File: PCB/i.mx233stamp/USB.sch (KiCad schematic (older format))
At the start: 36 parts, among them J3 USB_2A, J4 USB_2A, U4 GL850G, U5 RCLAMP0502B, U6 RCLAMP0502B, U7 RCLAMP0502B, U8 RCLAMP0502B, U9 MCP130, X2 12MHz

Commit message: Eliminación de los errores encontrados por el DRC
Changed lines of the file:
@@
-EESchema Schematic File Version 2  date Sat 13 Aug 2011 08:44:42 PM COT
+EESchema Schematic File Version 2  date Sun 14 Aug 2011 07:37:17 PM COT
 LIBS:con-jack
 LIBS:adm3101e
@@
 Sheet 2 4
 Title ""
-Date "14 aug 2011"
+Date "15 aug 2011"
 Rev ""
 Comp ""
@@
 Comment4 ""
 $EndDescr
+Connection ~ 1900 1600
+Connection ~ 1950 2850
+Connection ~ 1950 3150
+Connection ~ 1900 1900
 Text HLabel 2600 5250 0    60   BiDi ~ 0
 USB_P4

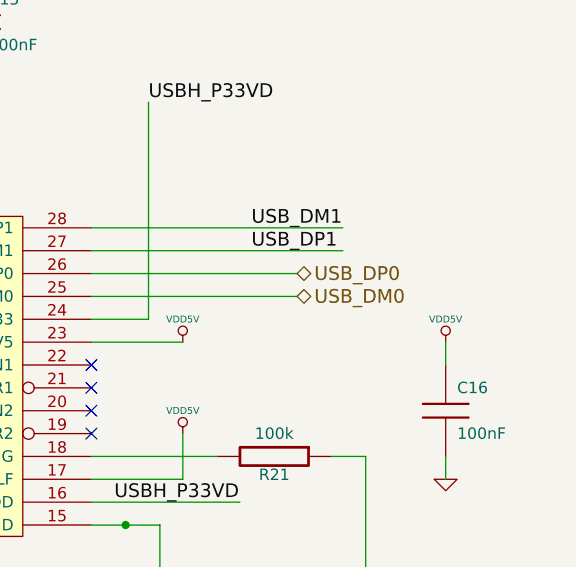
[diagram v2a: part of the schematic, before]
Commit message: Adición de jumpers que permitan el arranque USB
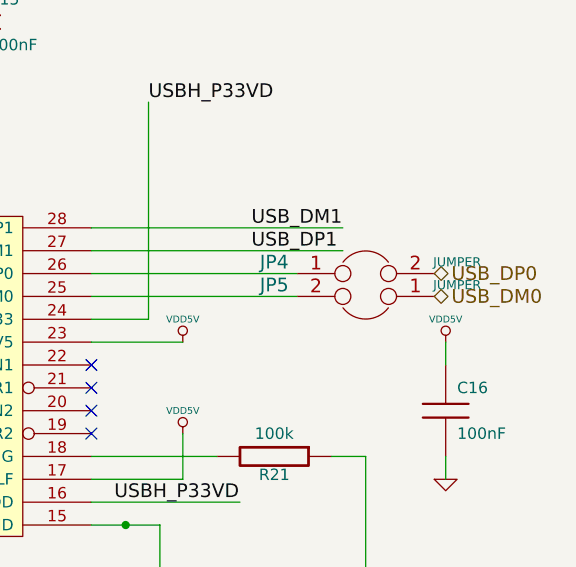
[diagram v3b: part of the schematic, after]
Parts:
- added JP4, JP5: JUMPER, PIN_ARRAY_2X1, symbol JUMPER

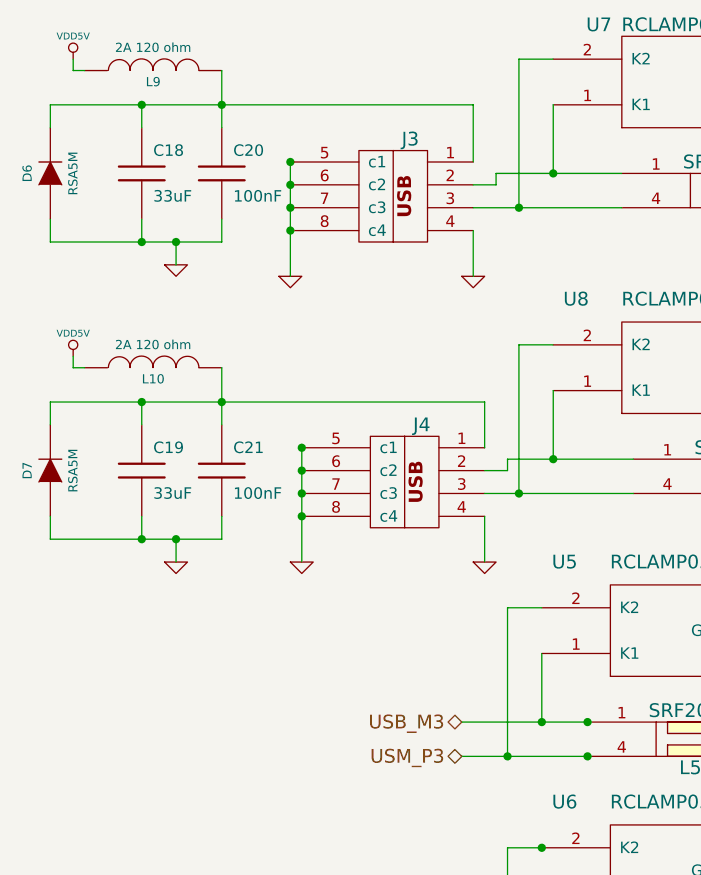
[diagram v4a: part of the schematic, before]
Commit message: LED0603 footprint has been fixed
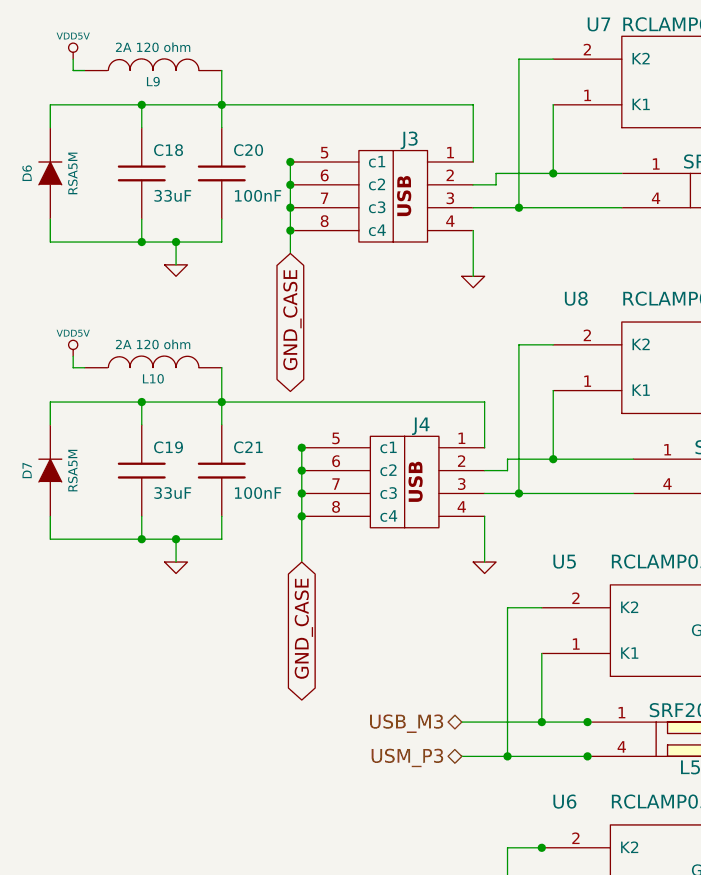
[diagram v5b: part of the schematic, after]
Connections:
- net labels added: GND_CASE
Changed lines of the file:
@@
-EESchema Schematic File Version 2  date Wed 17 Aug 2011 08:52:32 AM COT
+EESchema Schematic File Version 2  date Wed 17 Aug 2011 11:31:08 PM COT
 LIBS:con-jack
 LIBS:adm3101e
@@
 Sheet 2 4
 Title ""
-Date "17 aug 2011"
+Date "18 aug 2011"
 Rev ""
 Comp ""
@@
 Comment4 ""
 $EndDescr
+Wire Wire Line
+	1900 1600 1900 2000
 Connection ~ 1900 1600
 Connection ~ 1950 2850
@@
 Connection ~ 1900 1800
 Connection ~ 1900 1700
-Wire Wire Line
-	1900 1600 1900 2100
 Wire Wire Line
 	2700 1700 2800 1700
@@
 	5800 3550 5850 3550
 Connection ~ 5850 3550
+Text GLabel 1900 2000 3    60   BiDi ~ 0
+GND_CASE
+Text GLabel 1950 3350 3    60   BiDi ~ 0
+GND_CASE
 $Comp
 L JUMPER JP5
@@
 	1    0    0    -1
 $EndComp
-$Comp
-L GND #PWR02
-U 1 1 4E41CF8D
-P 1950 3350
-F 0 "#PWR02" H 1950 3350 30  0001 C CNN
-F 1 "GND" H 1950 3280 30  0001 C CNN
-	1    1950 3350
-	1    0    0    -1
-$EndComp
-$Comp
-L GND #PWR03
-U 1 1 4E41CF53
-P 1900 2100
-F 0 "#PWR03" H 1900 2100 30  0001 C CNN
-F 1 "GND" H 1900 2030 30  0001 C CNN
-	1    1900 2100
-	1    0    0    -1
-$EndComp
 Text Label 7150 3650 0    60   ~ 0
 USBH_P33VD
 $Comp
-L GND #PWR04
+L GND #PWR02
 U 1 1 4E41C8A5
 P 7300 3400
-F 0 "#PWR04" H 7300 3400 30  0001 C CNN
+F 0 "#PWR02" H 7300 3400 30  0001 C CNN
 F 1 "GND" H 7300 3330 30  0001 C CNN
 	1    7300 3400
@@
 $EndComp
 $Comp
-L GND #PWR05
+L GND #PWR03
 U 1 1 4E41C7BC
 P 6100 3800
-F 0 "#PWR05" H 6100 3800 30  0001 C CNN
+F 0 "#PWR03" H 6100 3800 30  0001 C CNN
 F 1 "GND" H 6100 3730 30  0001 C CNN
 	1    6100 3800
@@
 $EndComp
 $Comp
-L GND #PWR06
+L GND #PWR04
 U 1 1 4E4157F8
 P 4250 4850
-F 0 "#PWR06" H 4250 4850 30  0001 C CNN
+F 0 "#PWR04" H 4250 4850 30  0001 C CNN
 F 1 "GND" H 4250 4780 30  0001 C CNN
 	1    4250 4850
@@
 $EndComp
 $Comp
-L GND #PWR07
+L GND #PWR05
 U 1 1 4E4157E9
 P 4250 3800
-F 0 "#PWR07" H 4250 3800 30  0001 C CNN
+F 0 "#PWR05" H 4250 3800 30  0001 C CNN
 F 1 "GND" H 4250 3730 30  0001 C CNN
 	1    4250 3800
@@
 $EndComp
 $Comp
-L GND #PWR08
+L GND #PWR06
 U 1 1 4E4157C0
 P 4300 2650
-F 0 "#PWR08" H 4300 2650 30  0001 C CNN
+F 0 "#PWR06" H 4300 2650 30  0001 C CNN
 F 1 "GND" H 4300 2580 30  0001 C CNN
 	1    4300 2650
@@
 $EndComp
 $Comp
-L GND #PWR09
+L GND #PWR07
 U 1 1 4E4157B3
 P 4300 1350
-F 0 "#PWR09" H 4300 1350 30  0001 C CNN
+F 0 "#PWR07" H 4300 1350 30  0001 C CNN
 F 1 "GND" H 4300 1280 30  0001 C CNN
 	1    4300 1350
@@
 $EndComp
 $Comp
-L GND #PWR010
+L GND #PWR08
 U 1 1 4E41559E
 P 1400 3350
-F 0 "#PWR010" H 1400 3350 30  0001 C CNN
+F 0 "#PWR08" H 1400 3350 30  0001 C CNN
 F 1 "GND" H 1400 3280 30  0001 C CNN
 	1    1400 3350
@@
 $EndComp
 $Comp
-L GND #PWR011
+L GND #PWR09
 U 1 1 4E415157
 P 1400 2050
-F 0 "#PWR011" H 1400 2050 30  0001 C CNN
+F 0 "#PWR09" H 1400 2050 30  0001 C CNN
 F 1 "GND" H 1400 1980 30  0001 C CNN
 	1    1400 2050
@@
 $EndComp
 $Comp
-L VDD5V #PWR012
+L VDD5V #PWR010
 U 1 1 4E414F5E
 P 950 2450
-F 0 "#PWR012" H 950 2550 30  0001 C CNN
+F 0 "#PWR010" H 950 2550 30  0001 C CNN
 F 1 "VDD5V" H 950 2550 30  0000 C CNN
 	1    950  2450
@@
 $EndComp
 $Comp
-L GND #PWR013
+L GND #PWR011
 U 1 1 4E414F5D
 P 2750 3350
-F 0 "#PWR013" H 2750 3350 30  0001 C CNN
+F 0 "#PWR011" H 2750 3350 30  0001 C CNN
 F 1 "GND" H 2750 3280 30  0001 C CNN
 	1    2750 3350
@@
 $EndComp
 $Comp
-L GND #PWR014
+L GND #PWR012
 U 1 1 4E414F30
 P 2700 2100
-F 0 "#PWR014" H 2700 2100 30  0001 C CNN
+F 0 "#PWR012" H 2700 2100 30  0001 C CNN
 F 1 "GND" H 2700 2030 30  0001 C CNN
 	1    2700 2100
@@
 $EndComp
 $Comp
-L VDD5V #PWR015
+L VDD5V #PWR013
 U 1 1 4E414E3D
 P 950 1150
-F 0 "#PWR015" H 950 1250 30  0001 C CNN
+F 0 "#PWR013" H 950 1250 30  0001 C CNN
 F 1 "VDD5V" H 950 1250 30  0000 C CNN
 	1    950  1150
@@
 $EndComp
 $Comp
-L GND #PWR016
+L GND #PWR014
 U 1 1 4E3C4430
 P 10750 3150
-F 0 "#PWR016" H 10750 3150 30  0001 C CNN
+F 0 "#PWR014" H 10750 3150 30  0001 C CNN
 F 1 "GND" H 10750 3080 30  0001 C CNN
 	1    10750 3150
@@
 $EndComp
 $Comp
-L VDD5V #PWR017
+L VDD5V #PWR015
 U 1 1 4E3C4429
 P 10750 2550
-F 0 "#PWR017" H 10750 2650 30  0001 C CNN
+F 0 "#PWR015" H 10750 2650 30  0001 C CNN
 F 1 "VDD5V" H 10750 2650 30  0000 C CNN
 	1    10750 2550
@@
 $EndComp
 $Comp
-L VDD5V #PWR018
+L VDD5V #PWR016
 U 1 1 4E3C4418
 P 9600 2550
-F 0 "#PWR018" H 9600 2650 30  0001 C CNN
+F 0 "#PWR016" H 9600 2650 30  0001 C CNN
 F 1 "VDD5V" H 9600 2650 30  0000 C CNN
 	1    9600 2550
@@
 $EndComp
 $Comp
-L GND #PWR019
+L GND #PWR017
 U 1 1 4E3C436B
 P 8500 1650
-F 0 "#PWR019" H 8500 1650 30  0001 C CNN
+F 0 "#PWR017" H 8500 1650 30  0001 C CNN
 F 1 "GND" H 8500 1580 30  0001 C CNN
 	1    8500 1650
@@
 USBH_P33V
 $Comp
-L VDD5V #PWR020
+L VDD5V #PWR018
 U 1 1 4E3C4207
 P 9600 2950
-F 0 "#PWR020" H 9600 3050 30  0001 C CNN
+F 0 "#PWR018" H 9600 3050 30  0001 C CNN
 F 1 "VDD5V" H 9600 3050 30  0000 C CNN
 	1    9600 2950
@@
 USBH_P33V
 $Comp
-L GND #PWR021
+L GND #PWR019
 U 1 1 4E3C3A60
 P 9900 5600
-F 0 "#PWR021" H 9900 5600 30  0001 C CNN
+F 0 "#PWR019" H 9900 5600 30  0001 C CNN
 F 1 "GND" H 9900 5530 30  0001 C CNN
 	1    9900 5600
@@
 $EndComp
 $Comp
-L GND #PWR022
+L GND #PWR020
 U 1 1 4E3C3A56
 P 8000 5600
-F 0 "#PWR022" H 8000 5600 30  0001 C CNN
+F 0 "#PWR020" H 8000 5600 30  0001 C CNN
 F 1 "GND" H 8000 5530 30  0001 C CNN
 	1    8000 5600
@@
 andres.calderon@emqbit.com\n
 $Comp
-L GND #PWR023
+L GND #PWR021
 U 1 1 4E3C3807
 P 6500 2350
-F 0 "#PWR023" H 6500 2350 30  0001 C CNN
+F 0 "#PWR021" H 6500 2350 30  0001 C CNN
 F 1 "GND" H 6500 2280 30  0001 C CNN
 	1    6500 2350
@@
 $EndComp
 $Comp
-L GND #PWR024
+L GND #PWR022
 U 1 1 4E3C36BE
 P 10400 3600
-F 0 "#PWR024" H 10400 3600 30  0001 C CNN
+F 0 "#PWR022" H 10400 3600 30  0001 C CNN
 F 1 "GND" H 10400 3530 30  0001 C CNN
 	1    10400 3600
@@
 X1
 $Comp
-L GND #PWR025
+L GND #PWR023
 U 1 1 4E3C222B
 P 9500 3750
-F 0 "#PWR025" H 9500 3750 30  0001 C CNN
+F 0 "#PWR023" H 9500 3750 30  0001 C CNN
 F 1 "GND" H 9500 3680 30  0001 C CNN
 	1    9500 3750
@@
 USB_DM2
 $Comp
-L GND #PWR026
+L GND #PWR024
 U 1 1 4E3C212B
 P 5250 4300
-F 0 "#PWR026" H 5250 4300 30  0001 C CNN
+F 0 "#PWR024" H 5250 4300 30  0001 C CNN
 F 1 "GND" H 5250 4230 30  0001 C CNN
 	1    5250 4300
@@
 $EndComp
 $Comp
-L GND #PWR027
+L GND #PWR025
 U 1 1 4E3C206C
 P 5850 4300
-F 0 "#PWR027" H 5850 4300 30  0001 C CNN
+F 0 "#PWR025" H 5850 4300 30  0001 C CNN
 F 1 "GND" H 5850 4230 30  0001 C CNN
 	1    5850 4300
